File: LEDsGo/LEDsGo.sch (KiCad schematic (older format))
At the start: 47 parts, among them J1 USB_B_Micro, J2 AVR-ISP-6, SW0 SW_DIP_x01, SW1 SW_DIP_x01, SW2 SW_DIP_x01, SW3 SW_DIP_x01, SW4 SW_Push, SW5 SW_Push, SW6 SW_Push, SW7 SW_Push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

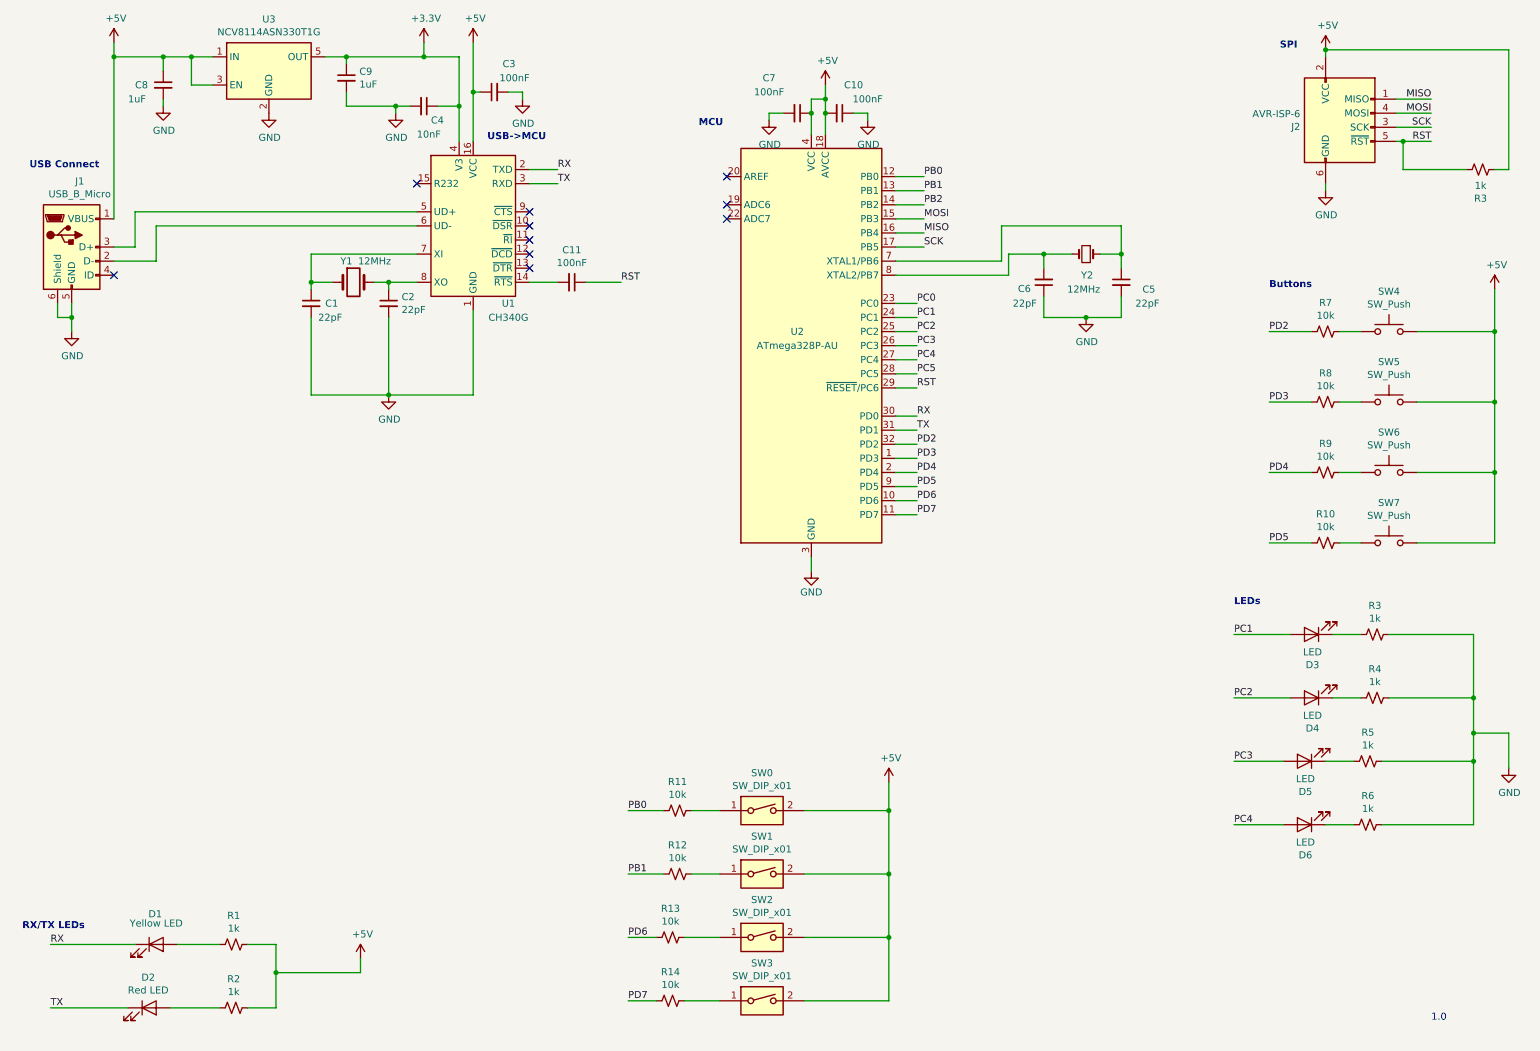
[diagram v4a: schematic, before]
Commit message: Added PDR to inputs, made some circuits more compact
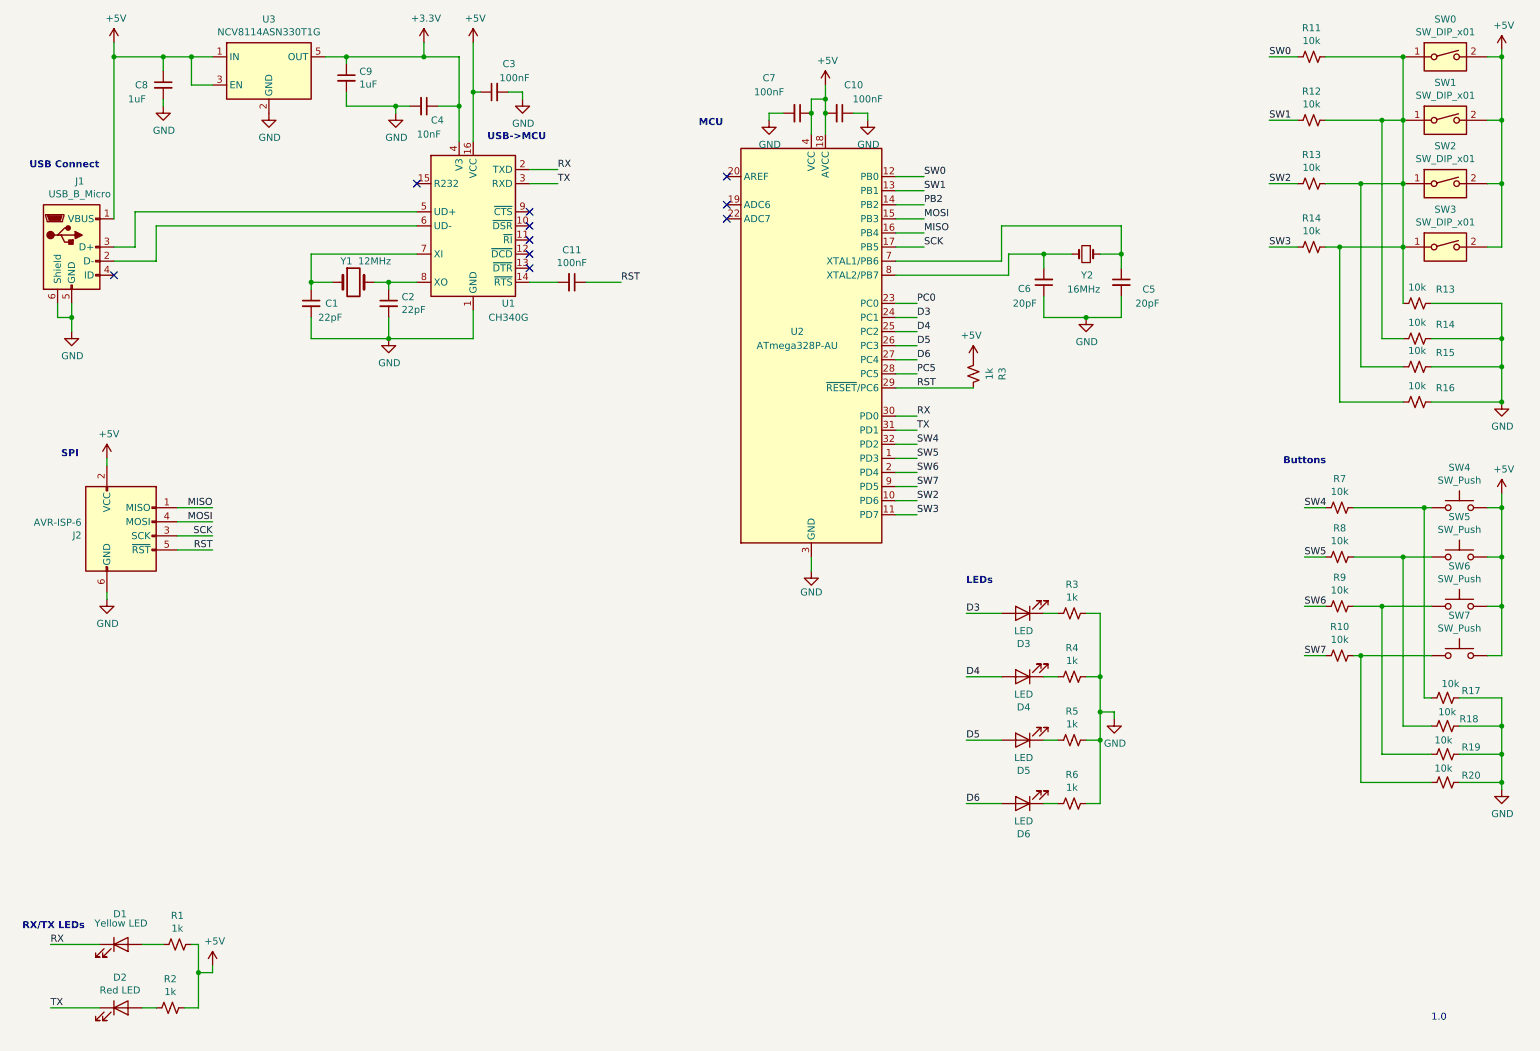
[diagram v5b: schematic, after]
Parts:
- added R13, R14, R15, R16, R17, R18, R19, R20: 10k, symbol Device:R_Small_US
- C5, C6: value 22pF -> 20pF
- Y2: value 12MHz -> 16MHz
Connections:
- net +5V: now also R3.2; no longer R3.1
- net GND: now also R13.2, R14.2, R15.2, R16.2, R17.1, R18.2, R19.1, R20.1
- net RST: now also R3.1; no longer R3.2
- net at R7.1, SW4.1: now also R17.2
- net at R8.1, SW5.1: now also R18.1
- net at R11.1, SW0.1: now also R12.1, R13.1, R14.1, SW1.1, SW2.1, SW3.1, R13.1, R14.1, R15.1, R16.1
- net at R9.1, SW6.1: now also R19.2
- net at R10.1, SW7.1: now also R20.2
- net PB0 renamed SW0
- net PB1 renamed SW1
- net PC1 renamed D3
- net PC2 renamed D4
- net PC3 renamed D5
- net PC4 renamed D6
- net PD2 renamed SW4
- net PD3 renamed SW5
- net PD4 renamed SW6
- net PD5 renamed SW7
- net PD6 renamed SW2
- net PD7 renamed SW3
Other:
- moved on the sheet: D1, D2, D3, D4, D5, D6, J2, R1, R10, R11, R12, R13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

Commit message: Cleaned some stuff up, added footprints
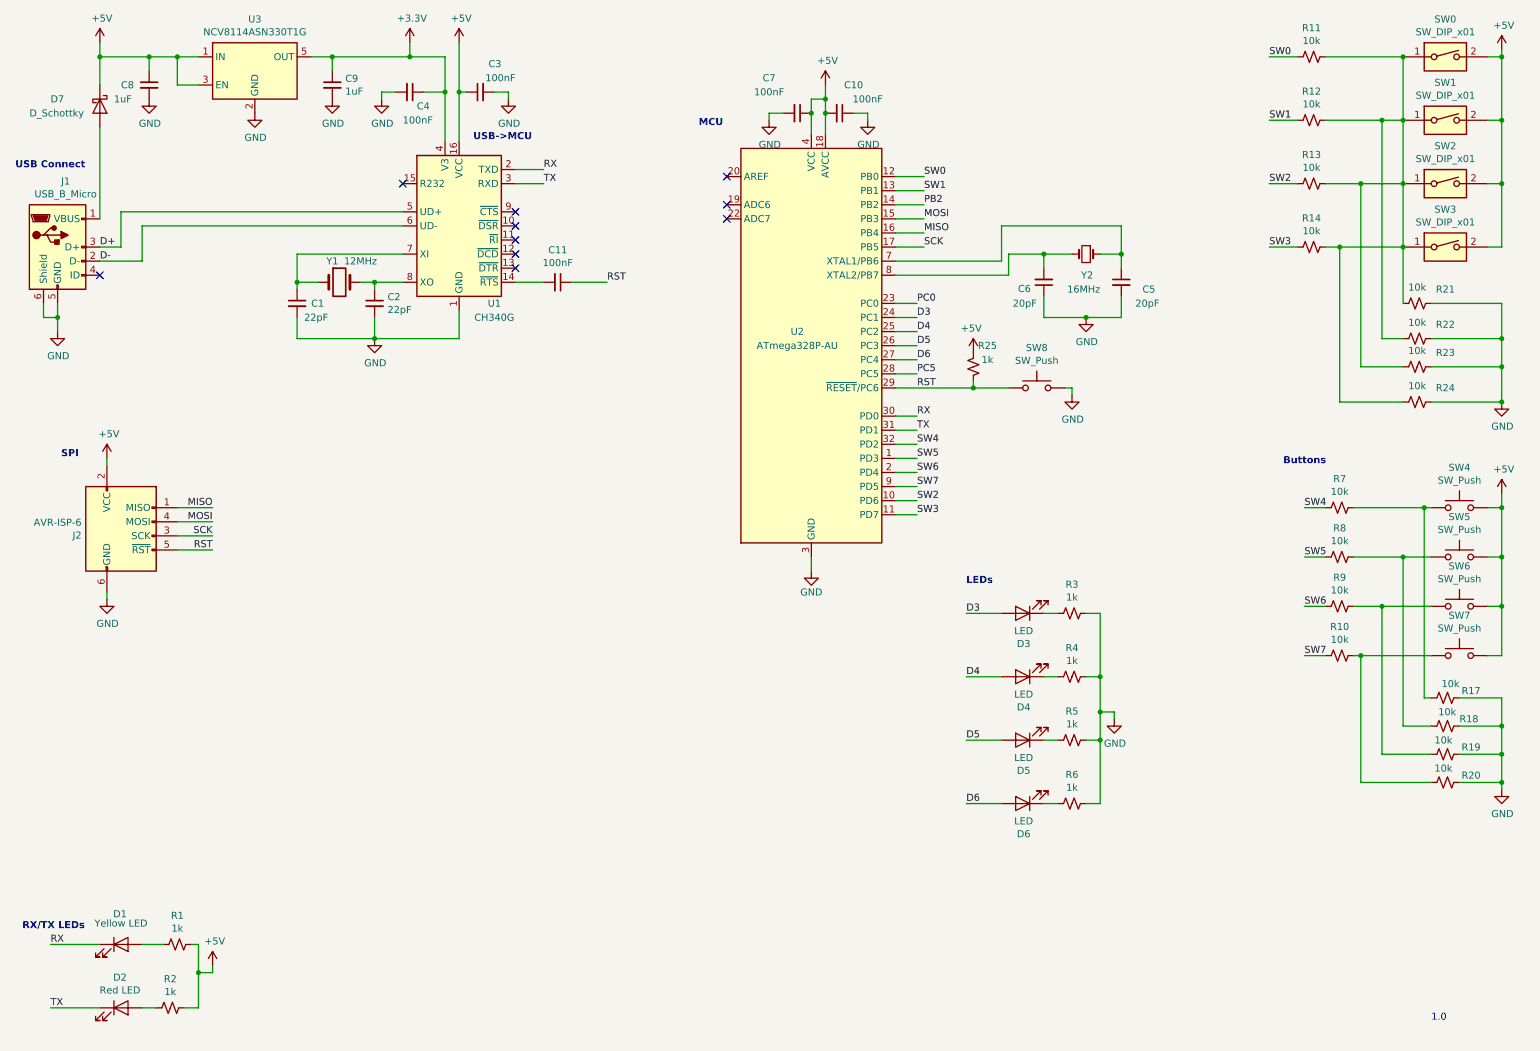
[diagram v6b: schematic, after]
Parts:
- added D7: D_Schottky, symbol Device:D_Schottky
- added SW8: SW_Push, symbol Switch:SW_Push
- C4: value 10nF -> 100nF
- D3, D4, D5, D6: footprint (none) -> LED_SMD:LED_0805_2012Metric
- R10, R11, R12, R13, R14, R17, R18, R19, R20, R3, R4, R5, R6, R7, R8, R9: footprint (none) -> Resistor_SMD:R_0805_2012Metric
- R21: renamed from R13; footprint (none) -> Resistor_SMD:R_0805_2012Metric
- R22: renamed from R14; footprint (none) -> Resistor_SMD:R_0805_2012Metric
- R23: renamed from R15; footprint (none) -> Resistor_SMD:R_0805_2012Metric
- R24: renamed from R16; footprint (none) -> Resistor_SMD:R_0805_2012Metric
- renumbered R3 to R25
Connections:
- net +5V: now also D7.1 (K); no longer J1.1 (VBUS)
- net GND: now also SW8.2
- net RST: now also SW8.1
- net D-: now reaches J1.2 (D-), U1.6 (UD-)
- net D+: now reaches J1.3 (D+), U1.5 (UD+)
- new net: D7.2 (A), J1.1 (VBUS)
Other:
- moved on the sheet: C1, C11, C2, C3, C4, C8, C9, J1, R25, U1, U3, Y1

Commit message: LED stuff
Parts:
- SW4, SW5, SW6, SW7: footprint (none) -> Button_Switch_THT:SW_PUSH_6mm
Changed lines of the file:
@@
 F 0 "SW4" H 10750 4285 50  0000 C CNN
 F 1 "SW_Push" H 10750 4194 50  0000 C CNN
-F 2 "" H 10750 4200 50  0001 C CNN
+F 2 "Button_Switch_THT:SW_PUSH_6mm" H 10750 4200 50  0001 C CNN
 F 3 "~" H 10750 4200 50  0001 C CNN
 	1    10750 4000
@@
 F 0 "SW5" H 10750 4635 50  0000 C CNN
 F 1 "SW_Push" H 10750 4544 50  0000 C CNN
-F 2 "" H 10750 4550 50  0001 C CNN
+F 2 "Button_Switch_THT:SW_PUSH_6mm" H 10750 4550 50  0001 C CNN
 F 3 "~" H 10750 4550 50  0001 C CNN
 	1    10750 4350
@@
 F 0 "SW6" H 10750 4985 50  0000 C CNN
 F 1 "SW_Push" H 10750 4894 50  0000 C CNN
-F 2 "" H 10750 4900 50  0001 C CNN
+F 2 "Button_Switch_THT:SW_PUSH_6mm" H 10750 4900 50  0001 C CNN
 F 3 "~" H 10750 4900 50  0001 C CNN
 	1    10750 4700
@@
 F 0 "SW7" H 10750 5335 50  0000 C CNN
 F 1 "SW_Push" H 10750 5244 50  0000 C CNN
-F 2 "" H 10750 5250 50  0001 C CNN
+F 2 "Button_Switch_THT:SW_PUSH_6mm" H 10750 5250 50  0001 C CNN
 F 3 "~" H 10750 5250 50  0001 C CNN
 	1    10750 5050
